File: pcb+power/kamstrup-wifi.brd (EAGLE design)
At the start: 36 x 81.3 mm, 23 parts, among them T1 BT137, T2 BT137

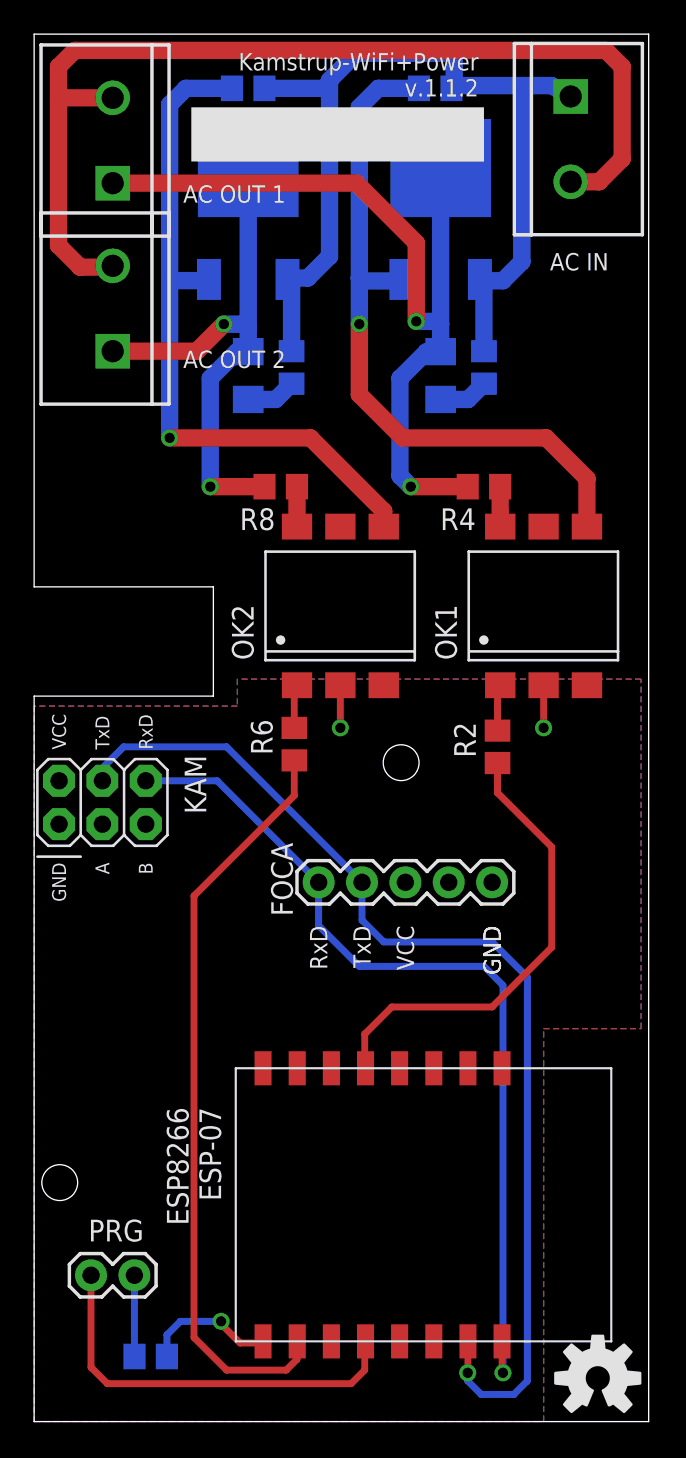
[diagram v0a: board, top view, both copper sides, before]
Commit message: pcb: v.1.1.4
better place for te terminal connectors
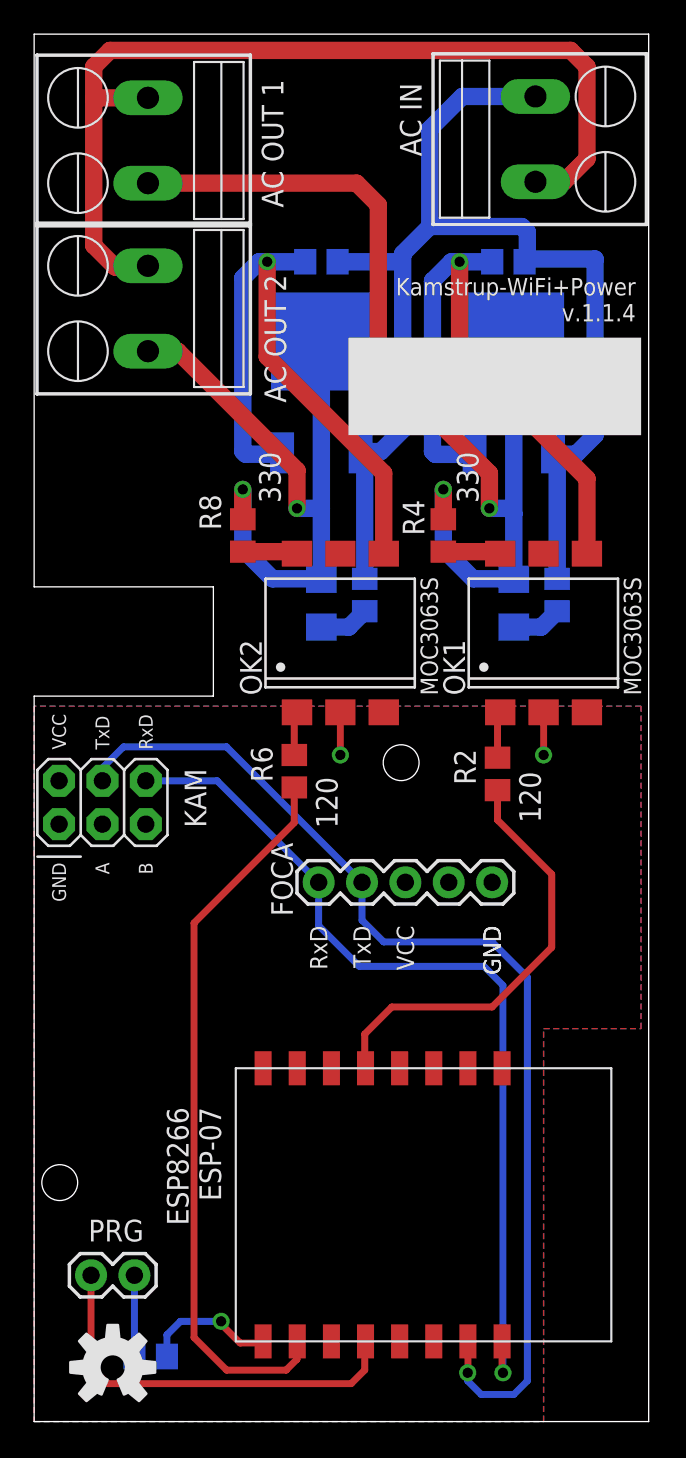
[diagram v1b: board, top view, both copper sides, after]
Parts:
- JP1, JP2, JP3: device SparkFun-Connectors:SCREWTERMINAL-5MM-2 -> TE Terminal Block 45 degrees:SCREWTERMINAL-5MM-2
- moved U$2 28.4 mm to (4.60, 3.17)
- moved C1 14.0 mm to (28.1, 47.9)
- moved C2 14.0 mm to (16.8, 47.9)
- moved R5 14.0 mm to (30.6, 48.4)
- moved R9 14.0 mm to (19.4, 48.4)
- moved R3 11.0 mm to (27.8, 67.9)
- moved R7 11.0 mm to (16.8, 67.9)
- moved T2 11.0 mm to (16.8, 59.8)
- moved T1 11.0 mm to (28.1, 59.8)
- moved R4 3.72 mm to (24.0, 51.9), turned to 90 degrees
- moved R8 3.62 mm to (12.2, 51.9), turned to 90 degrees
- moved JP1 2.06 mm to (29.4, 77.6)
- moved JP2 2.06 mm to (6.67, 72.5)
- moved JP3 2.06 mm to (6.67, 62.7)
- moved R2 1.59 mm to (27.1, 37.9)
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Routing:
- net N$9: track 55.2 -> 71.2 mm
- net N$15: track 49.1 -> 60.1 mm
- net N$8: track 31.6 -> 39.5 mm
- net N$13: track 41.6 -> 36.8 mm
- net N$6: track 41.1 -> 36.5 mm
- net N$18: track 60.2 -> 56.1 mm
- net N$16: track 44.4 -> 42.8 mm
- net N$11: track 27.2 -> 25.6 mm
- net N$14: track 2.34 -> 3.38 mm
- net N$7: track 2.34 -> 3.22 mm
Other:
- board text added: "Kamstrup-WiFi+Power v.1.1.4"
- board text added: "Part RS# C1, C2 766-1150 JP1, JP2, JP3 821-8701 KAM 702-2937 OK1, OK2 691-2319 R1 721-7820 R2, R6 721-6867 R3, R4, R7, R8 770-8742 R5, R9 770-8798 T1, T2 792-0709"
- board text removed: "Kamstrup-WiFi+Power v.1.1.2"

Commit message: pcb: v.1.1.5
more free area for antenna
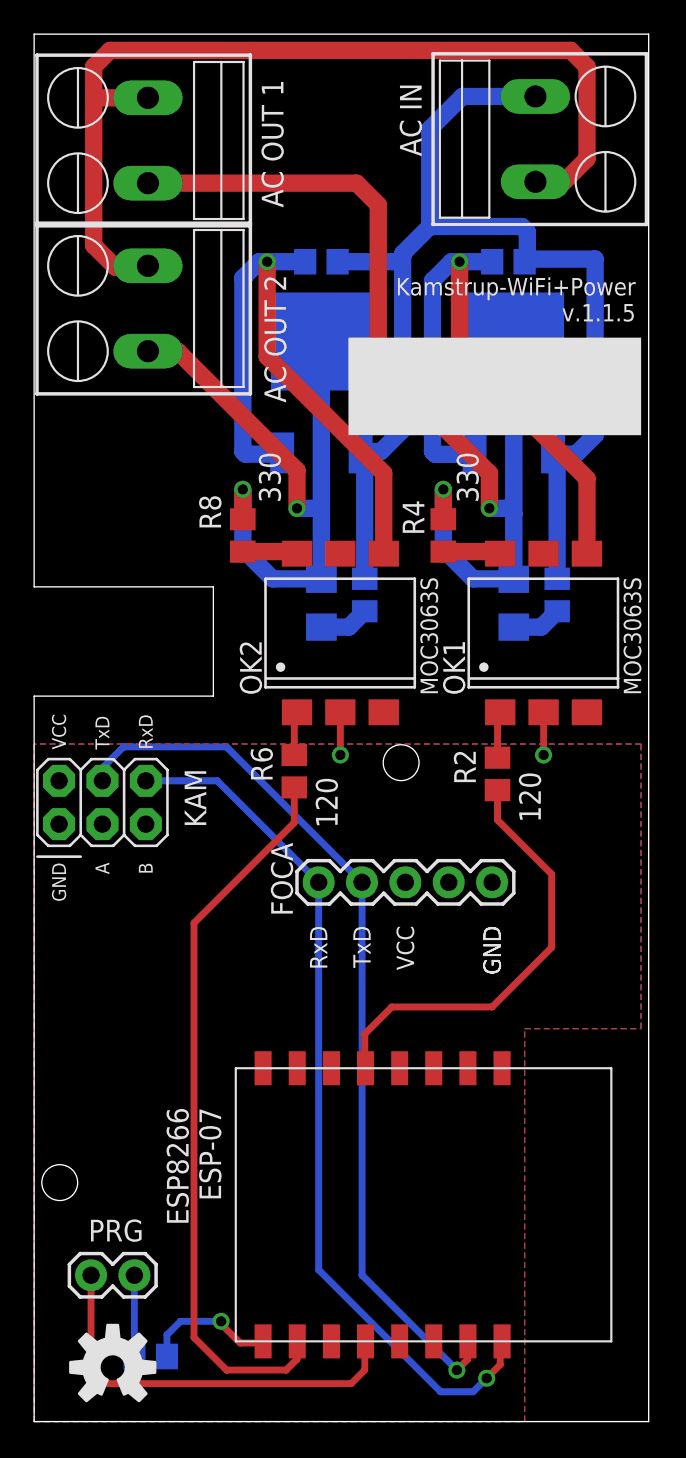
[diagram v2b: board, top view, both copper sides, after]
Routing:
- net N$2: track 63.2 -> 52.6 mm
- net N$1: track 51.9 -> 51.0 mm
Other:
- board text added: "Kamstrup-WiFi+Power v.1.1.5"
- board text removed: "Kamstrup-WiFi+Power v.1.1.4"
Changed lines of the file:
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@@
 ESP-07</text>
 <text x="35.2425" y="66.9925" size="1.016" layer="25" ratio="15" rot="R180">Kamstrup-WiFi+Power
-v.1.1.4</text>
+v.1.1.5</text>
 <text x="26.82875" y="29.05125" size="1.016" layer="25" rot="R90" align="center-right">GND</text>
 <text x="22.06625" y="78.4225" size="1.27" layer="25" ratio="20" rot="R90" align="center-right">AC IN</text>
@@
 <polygon width="0.4064" layer="16" isolate="0.4064">
 <vertex x="0" y="0"/>
-<vertex x="29.845" y="0"/>
-<vertex x="29.845" y="23.01875"/>
+<vertex x="28.73375" y="0"/>
+<vertex x="28.73375" y="23.01875"/>
 <vertex x="35.56" y="23.01875"/>
-<vertex x="35.56" y="41.91"/>
-<vertex x="0" y="41.91"/>
+<vertex x="35.56" y="39.6875"/>
+<vertex x="0" y="39.6875"/>
 </polygon>
 <contactref element="R1" pad="1"/>
@@
 <polygon width="0.4064" layer="1" isolate="0.4064">
 <vertex x="0" y="0"/>
-<vertex x="29.845" y="0"/>
-<vertex x="29.845" y="23.01875"/>
+<vertex x="28.73375" y="0"/>
+<vertex x="28.73375" y="23.01875"/>
 <vertex x="35.56" y="23.01875"/>
-<vertex x="35.56" y="41.91"/>
-<vertex x="0" y="41.91"/>
+<vertex x="35.56" y="39.6875"/>
+<vertex x="0" y="39.6875"/>
 </polygon>
 <contactref element="U$1" pad="CH_PD"/>
@@
 <contactref element="FOCA" pad="1"/>
 <contactref element="U$1" pad="TXD"/>
-<wire x1="27.4125" y1="4.7" x2="27.4125" y2="2.90875" width="0.4064" layer="1"/>
-<wire x1="27.4125" y1="2.90875" x2="27.46375" y2="2.8575" width="0.4064" layer="1"/>
-<via x="27.46375" y="2.8575" extent="1-16" drill="0.6"/>
-<wire x1="27.46375" y1="2.8575" x2="27.46375" y2="25.55875" width="0.4064" layer="16"/>
+<via x="26.51125" y="2.54" extent="1-16" drill="0.6"/>
 <wire x1="6.54" y1="37.54" x2="10.72" y2="37.54" width="0.4064" layer="16"/>
 <wire x1="10.72" y1="37.54" x2="16.66875" y2="31.59125" width="0.4064" layer="16"/>
-<wire x1="16.66875" y1="31.59125" x2="16.66875" y2="29.05125" width="0.4064" layer="16"/>
-<wire x1="27.46375" y1="25.55875" x2="26.3525" y2="26.67" width="0.4064" layer="16"/>
-<wire x1="26.3525" y1="26.67" x2="19.05" y2="26.67" width="0.4064" layer="16"/>
-<wire x1="19.05" y1="26.67" x2="16.66875" y2="29.05125" width="0.4064" layer="16"/>
+<wire x1="26.51125" y1="2.54" x2="27.305" y2="3.33375" width="0.4064" layer="1"/>
+<wire x1="27.305" y1="3.33375" x2="27.305" y2="4.5925" width="0.4064" layer="1"/>
+<wire x1="27.305" y1="4.5925" x2="27.4125" y2="4.7" width="0.4064" layer="1"/>
+<wire x1="26.51125" y1="2.54" x2="25.7175" y2="1.74625" width="0.4064" layer="16"/>
+<wire x1="25.7175" y1="1.74625" x2="23.8125" y2="1.74625" width="0.4064" layer="16"/>
+<wire x1="23.8125" y1="1.74625" x2="16.66875" y2="8.89" width="0.4064" layer="16"/>
+<wire x1="16.66875" y1="8.89" x2="16.66875" y2="31.59125" width="0.4064" layer="16"/>
 </signal>
 <signal name="N$2">
@@
 <contactref element="FOCA" pad="2"/>
 <contactref element="U$1" pad="RXD"/>
-<wire x1="25.4125" y1="4.7" x2="25.4125" y2="2.87" width="0.4064" layer="1"/>
-<wire x1="25.4125" y1="2.87" x2="25.4" y2="2.8575" width="0.4064" layer="1"/>
-<via x="25.4" y="2.8575" extent="1-16" drill="0.6"/>
-<wire x1="25.4" y1="2.8575" x2="25.4" y2="2.38125" width="0.4064" layer="16"/>
-<wire x1="25.4" y1="2.38125" x2="26.19375" y2="1.5875" width="0.4064" layer="16"/>
-<wire x1="26.19375" y1="1.5875" x2="28.09875" y2="1.5875" width="0.4064" layer="16"/>
-<wire x1="28.09875" y1="1.5875" x2="28.8925" y2="2.38125" width="0.4064" layer="16"/>
-<wire x1="28.8925" y1="2.38125" x2="28.8925" y2="26.035" width="0.4064" layer="16"/>
+<via x="24.765" y="3.01625" extent="1-16" drill="0.6"/>
 <wire x1="4" y1="37.54" x2="4" y2="38.29" width="0.4064" layer="16"/>
 <wire x1="4" y1="38.29" x2="5.23875" y2="39.52875" width="0.4064" layer="16"/>
 <wire x1="5.23875" y1="39.52875" x2="11.27125" y2="39.52875" width="0.4064" layer="16"/>
 <wire x1="11.27125" y1="39.52875" x2="19.20875" y2="31.59125" width="0.4064" layer="16"/>
-<wire x1="19.20875" y1="31.59125" x2="19.20875" y2="29.36875" width="0.4064" layer="16"/>
-<wire x1="19.20875" y1="29.36875" x2="20.47875" y2="28.09875" width="0.4064" layer="16"/>
-<wire x1="20.47875" y1="28.09875" x2="26.82875" y2="28.09875" width="0.4064" layer="16"/>
-<wire x1="26.82875" y1="28.09875" x2="28.8925" y2="26.035" width="0.4064" layer="16"/>
+<wire x1="25.4" y1="4.6875" x2="25.4125" y2="4.7" width="0.4064" layer="1"/>
+<wire x1="25.4" y1="4.6875" x2="25.4" y2="3.65125" width="0.4064" layer="1"/>
+<wire x1="25.4" y1="3.65125" x2="24.765" y2="3.01625" width="0.4064" layer="1"/>
+<wire x1="19.20875" y1="31.59125" x2="19.20875" y2="8.5725" width="0.4064" layer="16"/>
+<wire x1="19.20875" y1="8.5725" x2="24.765" y2="3.01625" width="0.4064" layer="16"/>
 </signal>
 <signal name="N$4">

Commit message: pcb: silk reordering
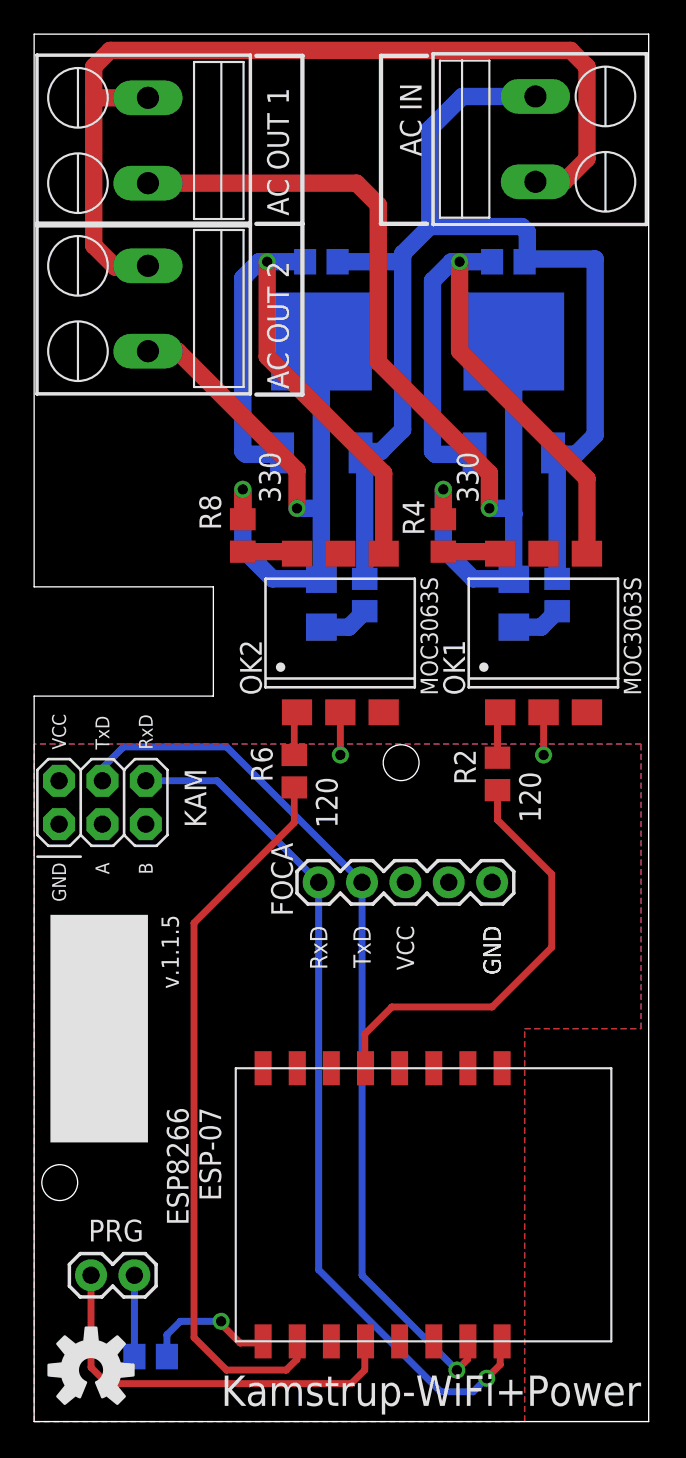
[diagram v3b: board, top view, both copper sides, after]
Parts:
- moved U$2 1.28 mm to (3.33, 3.02)
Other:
- board text added: "Kamstrup-WiFi+Power"
- board text added: "v.1.1.5"
- board text removed: "Kamstrup-WiFi+Power v.1.1.5"
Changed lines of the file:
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@@
 <layers>
 <layer number="1" name="Top" color="4" fill="1" visible="yes" active="yes"/>
-<layer number="16" name="Bottom" color="1" fill="1" visible="yes" active="yes"/>
+<layer number="16" name="Bottom" color="1" fill="1" visible="no" active="yes"/>
 <layer number="17" name="Pads" color="2" fill="1" visible="yes" active="yes"/>
 <layer number="18" name="Vias" color="2" fill="1" visible="yes" active="yes"/>
@@
 <layer number="20" name="Dimension" color="15" fill="1" visible="yes" active="yes"/>
 <layer number="21" name="tPlace" color="7" fill="1" visible="yes" active="yes"/>
-<layer number="22" name="bPlace" color="7" fill="1" visible="yes" active="yes"/>
+<layer number="22" name="bPlace" color="7" fill="1" visible="no" active="yes"/>
 <layer number="23" name="tOrigins" color="15" fill="1" visible="yes" active="yes"/>
-<layer number="24" name="bOrigins" color="15" fill="1" visible="yes" active="yes"/>
+<layer number="24" name="bOrigins" color="15" fill="1" visible="no" active="yes"/>
 <layer number="25" name="tNames" color="7" fill="1" visible="yes" active="yes"/>
-<layer number="26" name="bNames" color="7" fill="1" visible="yes" active="yes"/>
+<layer number="26" name="bNames" color="7" fill="1" visible="no" active="yes"/>
 <layer number="27" name="tValues" color="7" fill="1" visible="yes" active="yes"/>
-<layer number="28" name="bValues" color="7" fill="1" visible="yes" active="yes"/>
+<layer number="28" name="bValues" color="7" fill="1" visible="no" active="yes"/>
 <layer number="29" name="tStop" color="7" fill="3" visible="yes" active="yes"/>
-<layer number="30" name="bStop" color="7" fill="6" visible="yes" active="yes"/>
+<layer number="30" name="bStop" color="7" fill="6" visible="no" active="yes"/>
 <layer number="31" name="tCream" color="7" fill="4" visible="yes" active="yes"/>
-<layer number="32" name="bCream" color="7" fill="5" visible="yes" active="yes"/>
+<layer number="32" name="bCream" color="7" fill="5" visible="no" active="yes"/>
 <layer number="33" name="tFinish" color="6" fill="3" visible="yes" active="yes"/>
-<layer number="34" name="bFinish" color="6" fill="6" visible="yes" active="yes"/>
+<layer number="34" name="bFinish" color="6" fill="6" visible="no" active="yes"/>
 <layer number="35" name="tGlue" color="7" fill="4" visible="yes" active="yes"/>
-<layer number="36" name="bGlue" color="7" fill="5" visible="yes" active="yes"/>
+<layer number="36" name="bGlue" color="7" fill="5" visible="no" active="yes"/>
 <layer number="37" name="tTest" color="7" fill="1" visible="yes" active="yes"/>
-<layer number="38" name="bTest" color="7" fill="1" visible="yes" active="yes"/>
+<layer number="38" name="bTest" color="7" fill="1" visible="no" active="yes"/>
 <layer number="39" name="tKeepout" color="4" fill="11" visible="yes" active="yes"/>
-<layer number="40" name="bKeepout" color="1" fill="11" visible="yes" active="yes"/>
+<layer number="40" name="bKeepout" color="1" fill="11" visible="no" active="yes"/>
 <layer number="41" name="tRestrict" color="4" fill="10" visible="yes" active="yes"/>
-<layer number="42" name="bRestrict" color="1" fill="10" visible="yes" active="yes"/>
+<layer number="42" name="bRestrict" color="1" fill="10" visible="no" active="yes"/>
 <layer number="43" name="vRestrict" color="2" fill="10" visible="yes" active="yes"/>
 <layer number="44" name="Drills" color="7" fill="1" visible="yes" active="yes"/>
@@
 <layer number="50" name="dxf" color="7" fill="1" visible="no" active="no"/>
 <layer number="51" name="tDocu" color="7" fill="1" visible="yes" active="yes"/>
-<layer number="52" name="bDocu" color="7" fill="1" visible="yes" active="yes"/>
+<layer number="52" name="bDocu" color="7" fill="1" visible="no" active="yes"/>
 <layer number="53" name="tGND_GNDA" color="7" fill="9" visible="no" active="no"/>
 <layer number="54" name="bGND_GNDA" color="1" fill="9" visible="no" active="no"/>
@@
 <layer number="104" name="Name" color="16" fill="1" visible="yes" active="yes"/>
 <layer number="105" name="tPlate" color="7" fill="1" visible="yes" active="yes"/>
-<layer number="106" name="bPlate" color="7" fill="1" visible="yes" active="yes"/>
+<layer number="106" name="bPlate" color="7" fill="1" visible="no" active="yes"/>
 <layer number="107" name="Crop" color="7" fill="1" visible="yes" active="yes"/>
 <layer number="108" name="tplace-old" color="10" fill="1" visible="no" active="yes"/>
@@
 <layer number="116" name="Patch_BOT" color="9" fill="4" visible="yes" active="yes"/>
 <layer number="121" name="_tsilk" color="7" fill="1" visible="yes" active="yes"/>
-<layer number="122" name="_bsilk" color="7" fill="1" visible="yes" active="yes"/>
+<layer number="122" name="_bsilk" color="7" fill="1" visible="no" active="yes"/>
 <layer number="123" name="tTestmark" color="7" fill="1" visible="no" active="yes"/>
 <layer number="124" name="bTestmark" color="7" fill="1" visible="no" active="yes"/>
@@
 <text x="7.77875" y="18.415" size="1.27" layer="25" ratio="10" rot="R270">ESP8266
 ESP-07</text>
-<text x="35.2425" y="66.9925" size="1.016" layer="25" ratio="15" rot="R180">Kamstrup-WiFi+Power
-v.1.1.5</text>
+<text x="7.46125" y="29.68625" size="1.016" layer="25" ratio="15" rot="R270">v.1.1.5</text>
 <text x="26.82875" y="29.05125" size="1.016" layer="25" rot="R90" align="center-right">GND</text>
 <text x="22.06625" y="78.4225" size="1.27" layer="25" ratio="20" rot="R90" align="center-right">AC IN</text>
-<text x="13.97" y="71.12" size="1.27" layer="25" ratio="20" rot="R90" align="center-left">AC OUT 1</text>
-<text x="14.12875" y="59.69" size="1.27" layer="25" ratio="20" rot="R90" align="center-left">AC OUT 2</text>
-<rectangle x1="18.415" y1="57.785" x2="35.56" y2="63.5" layer="25"/>
+<text x="14.2875" y="70.64375" size="1.27" layer="25" ratio="20" rot="R90" align="center-left">AC OUT 1</text>
+<text x="14.2875" y="60.48375" size="1.27" layer="25" ratio="20" rot="R90" align="center-left">AC OUT 2</text>
 <text x="27.6225" y="13.0175" size="1.016" layer="26" font="fixed" rot="MR0">Part            RS#
 C1, C2          766-1150
@@
 <wire x1="28.41625" y1="13.81125" x2="28.41625" y2="29.845" width="0.1524" layer="26"/>
 <wire x1="14.2875" y1="29.845" x2="14.2875" y2="13.81125" width="0.1524" layer="26"/>
+<wire x1="13.0175" y1="80.01" x2="15.71625" y2="80.01" width="0.254" layer="25"/>
+<wire x1="15.71625" y1="80.01" x2="15.71625" y2="70.1675" width="0.254" layer="25"/>
+<wire x1="15.71625" y1="70.1675" x2="15.71625" y2="60.16625" width="0.254" layer="25"/>
+<wire x1="15.71625" y1="60.16625" x2="13.0175" y2="60.16625" width="0.254" layer="25"/>
+<wire x1="15.71625" y1="70.1675" x2="13.0175" y2="70.1675" width="0.254" layer="25"/>
+<wire x1="20.32" y1="80.01" x2="23.01875" y2="80.01" width="0.254" layer="25"/>
+<wire x1="20.32" y1="70.1675" x2="23.01875" y2="70.1675" width="0.254" layer="25"/>
+<wire x1="20.32" y1="80.01" x2="20.32" y2="70.1675" width="0.254" layer="25"/>
+<text x="35.56" y="2.69875" size="1.778" layer="25" ratio="15" rot="R180">Kamstrup-WiFi+Power</text>
+<rectangle x1="0.9525" y1="16.35125" x2="6.6675" y2="29.68625" layer="25"/>
 </plain>
 <attributes>
@@
 <attribute name="NAME" x="6.4262" y="11.8237" size="1.27" layer="25" ratio="10" rot="R180"/>
 </element>
-<element name="U$2" library="SparkFun-Aesthetics" package="OSHW-LOGO-M" value="" x="4.60375" y="3.175"/>
+<element name="U$2" library="SparkFun-Aesthetics" package="OSHW-LOGO-M" value="" x="3.33375" y="3.01625"/>
 <element name="R1" library="rcl" package="R0805" value="10k" x="6.82625" y="3.81" smashed="yes" rot="MR0">
 <attribute name="NAME" x="8.73125" y="5.23875" size="1.27" layer="26" rot="MR0"/>
